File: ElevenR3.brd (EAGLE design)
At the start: 68.6 x 53.3 mm, 63 parts, among them IC1 ATMEGA328P, IC2 ATMEGA16U2-MU, IC3 MC33269DT-5.0, IC4 LM358D, IC5 LP2985-33DBVR, J2 Analog, J3 Digital_8_13, J4 Digital_0_7, J5 DC_2_1MM, J6 Digital_0_7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

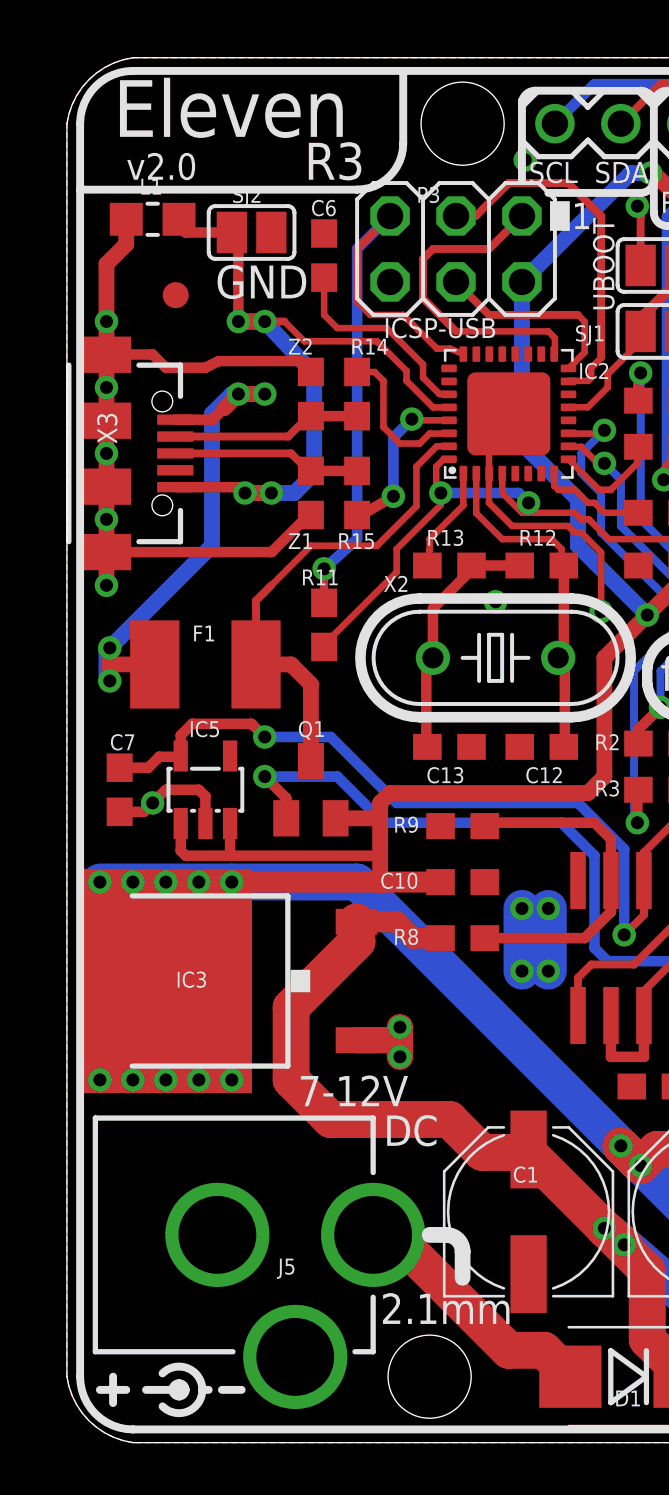
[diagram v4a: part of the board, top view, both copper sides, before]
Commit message: Replaced uUSB footprint
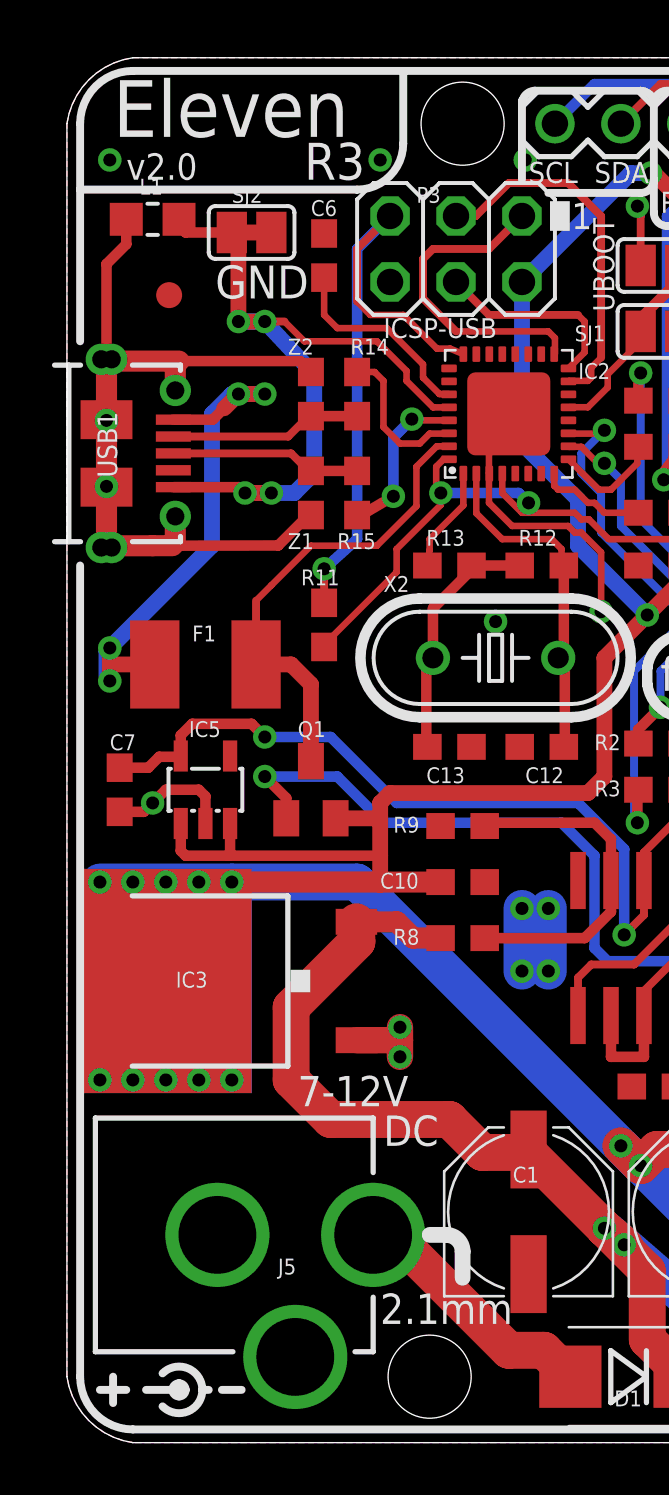
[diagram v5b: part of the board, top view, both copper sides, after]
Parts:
- removed X3: USBSF-MICROB, freetronics-jon:USB-MICROB
- added USB1: USB-6PSMT, freetronics-jon:USB-MICROB-MB05PMXX
- moved U$5 0.25 mm to (3.94, 44.2)
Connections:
- net N$115: now also USB1.VBUS; no longer X3.VBUS
- net N$16: now also USB1.D+; no longer X3.D+
- net N$17: now also USB1.D-; no longer X3.D-
- net N$3: now also USB1.FIX1, USB1.FIX2, USB1.PIN1, USB1.PIN2, USB1.TAB1, USB1.TAB2; no longer X3.FIX1, X3.FIX2, X3.TAB1, X3.TAB2
- net UGND: now also USB1.GND; no longer X3.GND
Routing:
- net N$3: track 31.2 -> 34.2 mm, vias 5 -> 2
- net N$116: track 0.00 -> 1.52 mm
- net GND: vias 15 -> 17
